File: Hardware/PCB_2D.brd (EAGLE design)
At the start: 171.2 x 110.2 mm, 103 parts, among them IC1 XC6220A331MR-G, IC2 BD5229G-TR, J1 SAMACSYS_PARTS_USB4110-GF-A, J2 QWIIC_RIGHT_ANGLE, J3 FH34SRJ-24S-0.5SH_99_, J4 112A-TAAR-R03_ATTENDPACHET, Q1 20V/4.2A/52mΩ/1.4W, Q2 SI1308EDL-T1-GE3, Q3 20V/4.2A/52mΩ/1.4W, U1 ESP32-C6-WROOM-1-N8, U2 MAX17048G+T10, U3 W25Q512JVEIQ, U4 DS3231SN#

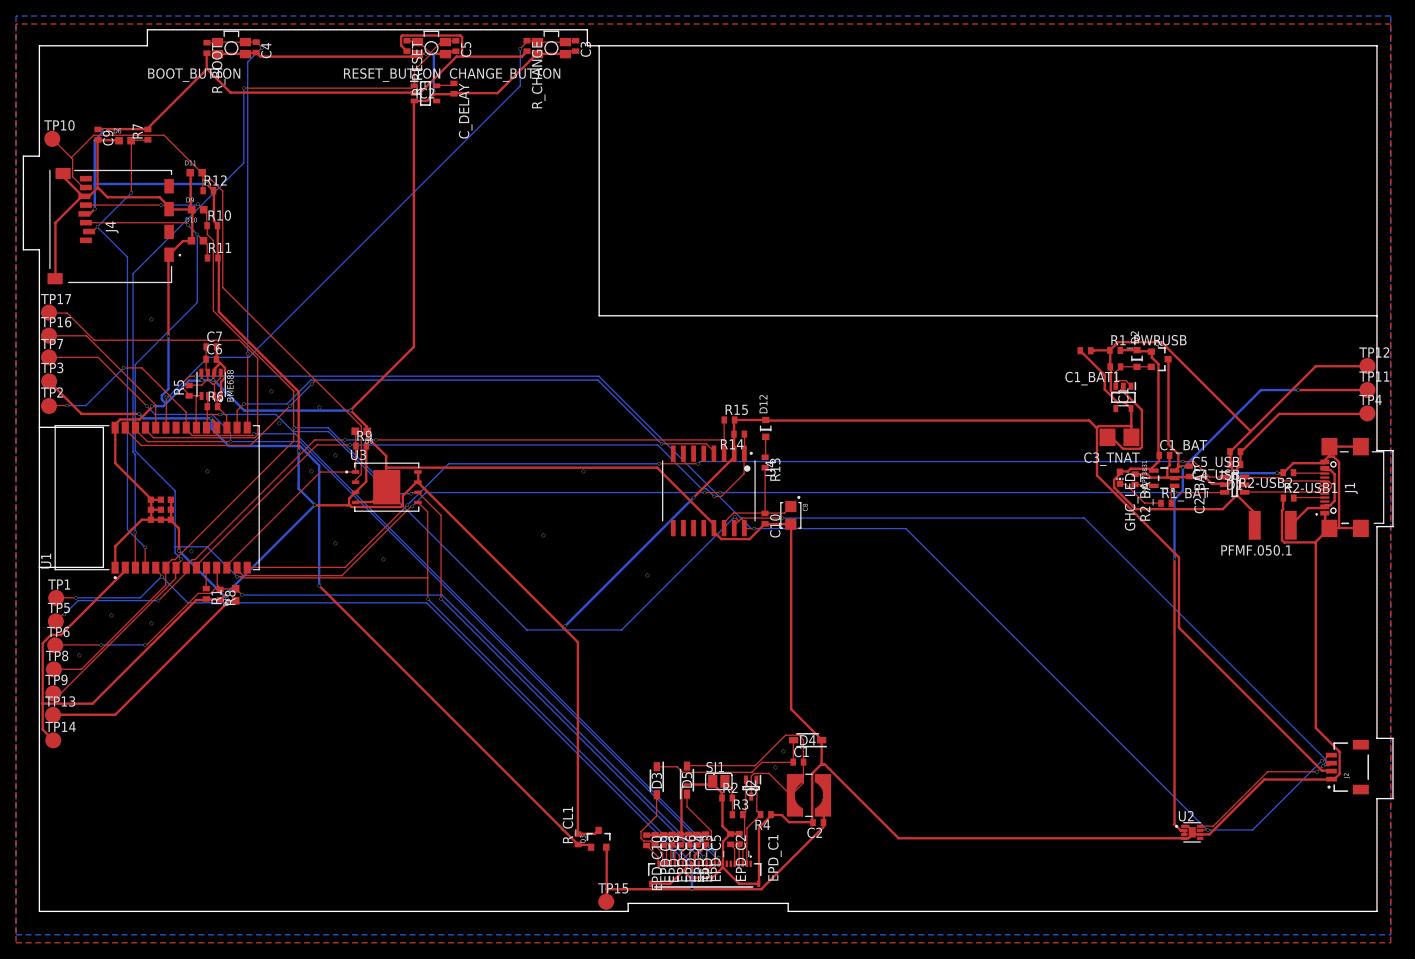
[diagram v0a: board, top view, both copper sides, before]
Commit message: Fixes #1. #2. #3. #4. #5. #6. #7 #8 #9: Improved 3D models, silkscreen and schematic
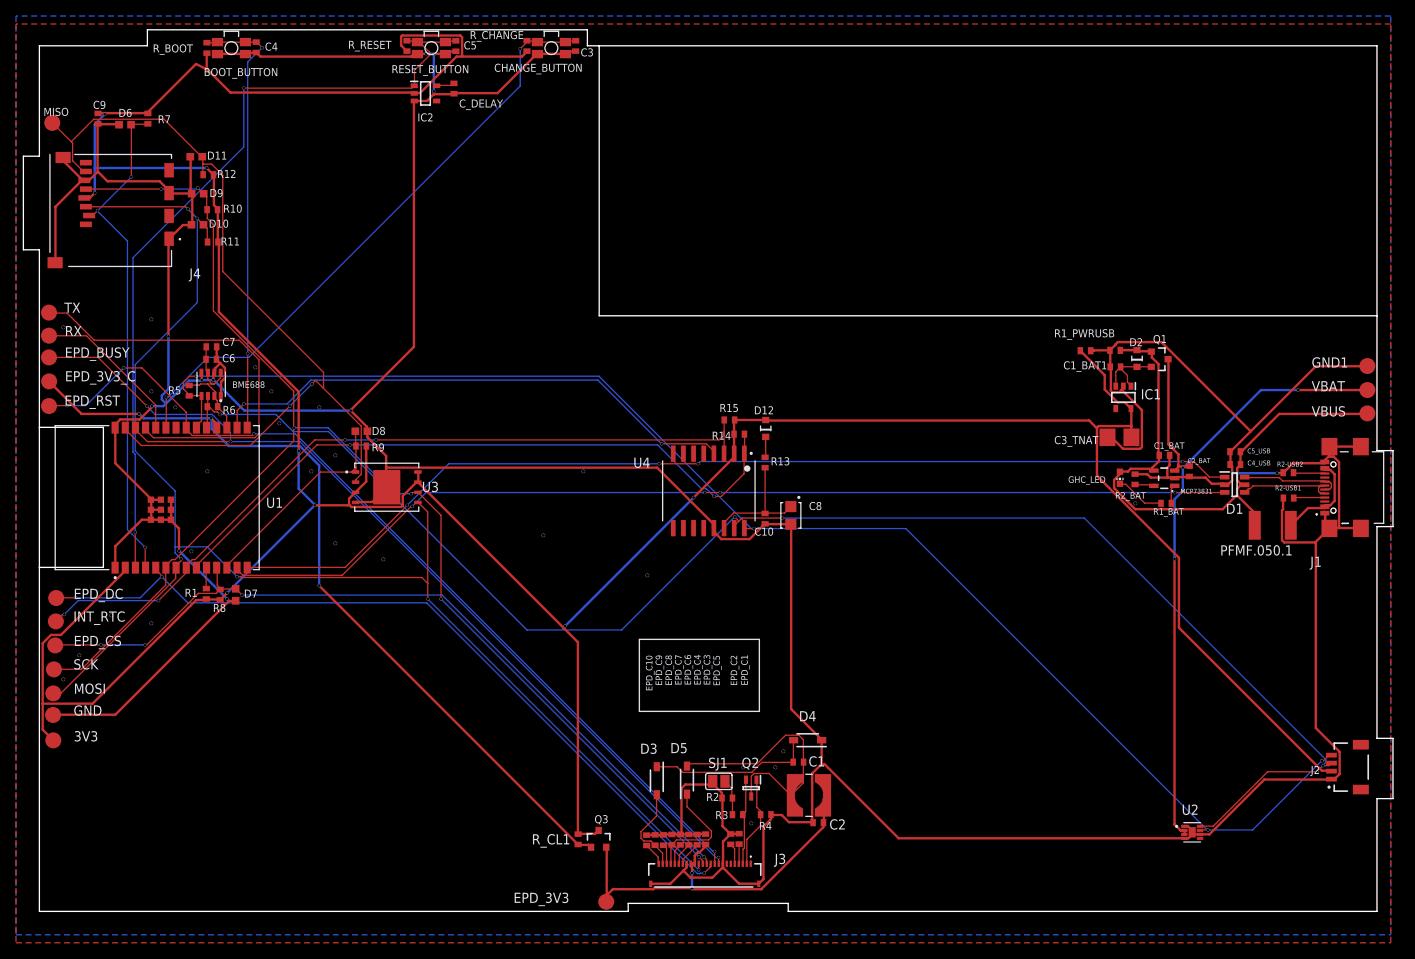
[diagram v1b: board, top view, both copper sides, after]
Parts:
- removed TP10: TPTP20R, DeskAssistant v19 v1:TP20R
- added MISO: TPTP20R, DeskAssistant v19 v1:TP20R
- moved C9 2.00 mm to (7.33, 99.1)
- moved D10 2.00 mm to (19.8, 85.8)
- moved D11 2.00 mm to (19.6, 94.3)
- moved D6 2.00 mm to (10.7, 98.3)
- moved D9 2.00 mm to (19.8, 89.7)
- moved J4 2.00 mm to (5.82, 94.7)
- moved R10 2.00 mm to (21.6, 87.7)
- moved R11 2.00 mm to (21.7, 83.7)
- moved R12 2.00 mm to (21.1, 92.1)
- moved R7 2.00 mm to (13.6, 99.1)
- renumbered TP1 to EPD_DC, TP11 to VBAT, TP12 to GND1, TP13 to GND, TP14 to 3V3, TP15 to EPD_3V3, TP16 to RX, TP17 to TX, TP2 to EPD_RST, TP3 to EPD_3V3_C, TP4 to VBUS, TP5 to INT_RTC, TP6 to EPD_CS, TP7 to EPD_BUSY, TP8 to SCK, TP9 to MOSI
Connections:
- net MISO: now also MISO.TP; no longer TP10.TP
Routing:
- net MISO: track 105.0 -> 108.3 mm
- net MOSI: track 182.6 -> 184.9 mm
- net GND: track 698.4 -> 700.4 mm, vias 31 -> 38
- net SS_SD: track 61.1 -> 63.1 mm
- net SCK: track 172.1 -> 174.1 mm
- net 3V3: track 452.3 -> 453.9 mm
- net I2C_PW: track 15.7 -> 17.3 mm
- net RESET: track 99.6 -> 100.3 mm
- net INT_RTC: track 97.7 -> 98.4 mm
- net N$3: track 8.74 -> 9.37 mm
